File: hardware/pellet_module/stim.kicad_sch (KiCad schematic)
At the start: 17 parts, among them J11 Conn_Coaxial, J12 Conn_01x02_Pin, J13 Conn_01x02_Pin, J14 Conn_01x02_Pin, J15 Conn_Coaxial, J16 Conn_Coaxial, J17 Conn_Coaxial, J18 Conn_Coaxial, J21 Conn_Coaxial, U7 TXB0104RUT

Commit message: make updated pellet step for alogus
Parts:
- J12, J13, J14: footprint Connector_PinHeader_2.54mm:PinHeader_1x02_P2.54mm_Horizontal -> Connector_Molex:Molex_PicoBlade_53048-0210_1x02_P1.25mm_Horizontal; LCSC C225269 -> C505099; MPN A2005WR-2P -> 0530480210
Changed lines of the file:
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@@
+	(symbol
+		(lib_id "Connector:Conn_01x02_Pin")
+		(at 59.69 116.84 0)
+		(mirror y)
+		(unit 1)
+		(exclude_from_sim no)
+		(in_bom yes)
+		(on_board yes)
+		(dnp no)
+		(fields_autoplaced yes)
+		(property "Reference" "J14"
+			(at 60.96 116.8399 0)
+			(effects
+				(font
+					(size 1.27 1.27)
+				)
+				(justify right)
+			)
+		)
+		(property "Value" "Conn_01x02_Pin"
+			(at 60.96 119.3799 0)
+			(effects
+				(font
+					(size 1.27 1.27)
+				)
+				(justify right)
+			)
+		)
+		(property "Footprint" "Connector_Molex:Molex_PicoBlade_53048-0210_1x02_P1.25mm_Horizontal"
+			(at 59.69 116.84 0)
+			(effects
+				(font
+					(size 1.27 1.27)
+				)
+				(hide yes)
+			)
+		)
+		(property "Datasheet" "~"
+			(at 59.69 116.84 0)
+			(effects
+				(font
+					(size 1.27 1.27)
+				)
+				(hide yes)
+			)
+		)
+		(property "Description" "Generic connector, single row, 01x02, script generated"
+			(at 59.69 116.84 0)
+			(effects
+				(font
+					(size 1.27 1.27)
+				)
+				(hide yes)
+			)
+		)
+		(property "MPN" "0530480210"
+			(at 59.69 116.84 0)
+			(effects
+				(font
+					(size 1.27 1.27)
+				)
+				(hide yes)
+			)
+		)
+		(property "LCSC" "C505099"
+			(at 59.69 116.84 0)
+			(effects
+				(font
+					(size 1.27 1.27)
+				)
+				(hide yes)
+			)
+		)
+		(pin "2"
+		)
+		(pin "1"
+		)
+		(instances
+			(project "pellet"
+				(path "/48650363-a452-429d-997e-1ddabb69aad0/b8597be6-0cb3-4e54-9f55-240b87344e85"
+					(reference "J14")
+					(unit 1)
+				)
+			)
+		)
+	)
 	(symbol
 		(lib_id "Connector:Conn_01x02_Pin")
@@
 			)
 		)
-		(property "Footprint" "Connector_PinHeader_2.54mm:PinHeader_1x02_P2.54mm_Horizontal"
+		(property "Footprint" "Connector_Molex:Molex_PicoBlade_53048-0210_1x02_P1.25mm_Horizontal"
 			(at 59.69 101.6 0)
 			(effects
@@
 			)
 		)
-		(property "MPN" " A2005WR-2P"
+		(property "MPN" "0530480210"
 			(at 59.69 101.6 0)
 			(effects
@@
 			)
 		)
-		(property "LCSC" "C225269"
+		(property "LCSC" "C505099"
 			(at 59.69 101.6 0)
 			(effects
@@
 			)
 		)
-		(property "Footprint" "Connector_PinHeader_2.54mm:PinHeader_1x02_P2.54mm_Horizontal"
+		(property "Footprint" "Connector_Molex:Molex_PicoBlade_53048-0210_1x02_P1.25mm_Horizontal"
 			(at 59.69 86.36 0)
 			(effects
@@
 			)
 		)
-		(property "MPN" " A2005WR-2P"
+		(property "MPN" "0530480210"
 			(at 59.69 86.36 0)
 			(effects
@@
 			)
 		)
-		(property "LCSC" "C225269"
+		(property "LCSC" "C505099"
 			(at 59.69 86.36 0)
 			(effects
@@
 					(unit 1)
 				)
-			)
-		)
-	)
-	(symbol
-		(lib_id "Connector:Conn_01x02_Pin")
-		(at 59.69 116.84 0)
-		(mirror y)
-		(unit 1)
-		(exclude_from_sim no)
-		(in_bom yes)
-		(on_board yes)
-		(dnp no)
-		(fields_autoplaced yes)
-		(property "Reference" "J14"
-			(at 60.96 116.8399 0)
-			(effects
-				(font
-					(size 1.27 1.27)
-				)
-				(justify right)
-			)
-		)
-		(property "Value" "Conn_01x02_Pin"
-			(at 60.96 119.3799 0)
-			(effects
-				(font
-					(size 1.27 1.27)
-				)
-				(justify right)
-			)
-		)
-		(property "Footprint" "Connector_PinHeader_2.54mm:PinHeader_1x02_P2.54mm_Horizontal"
-			(at 59.69 116.84 0)
-			(effects
-				(font
-					(size 1.27 1.27)
-				)
-				(hide yes)
-			)
-		)
-		(property "Datasheet" "~"
-			(at 59.69 116.84 0)
-			(effects
-				(font
-					(size 1.27 1.27)
-				)
-				(hide yes)
-			)
-		)
-		(property "Description" "Generic connector, single row, 01x02, script generated"
-			(at 59.69 116.84 0)
-			(effects
-				(font
-					(size 1.27 1.27)
-				)
-				(hide yes)
-			)
-		)
-		(property "MPN" " A2005WR-2P"
-			(at 59.69 116.84 0)
-			(effects
-				(font
-					(size 1.27 1.27)
-				)
-				(hide yes)
-			)
-		)
-		(property "LCSC" "C225269"
-			(at 59.69 116.84 0)
-			(effects
-				(font
-					(size 1.27 1.27)
-				)
-				(hide yes)
-			)
-		)
-		(pin "2"
-		)
-		(pin "1"
-		)
-		(instances
-			(project "pellet"
-				(path "/48650363-a452-429d-997e-1ddabb69aad0/b8597be6-0cb3-4e54-9f55-240b87344e85"
-					(reference "J14")
-					(unit 1)
-				)

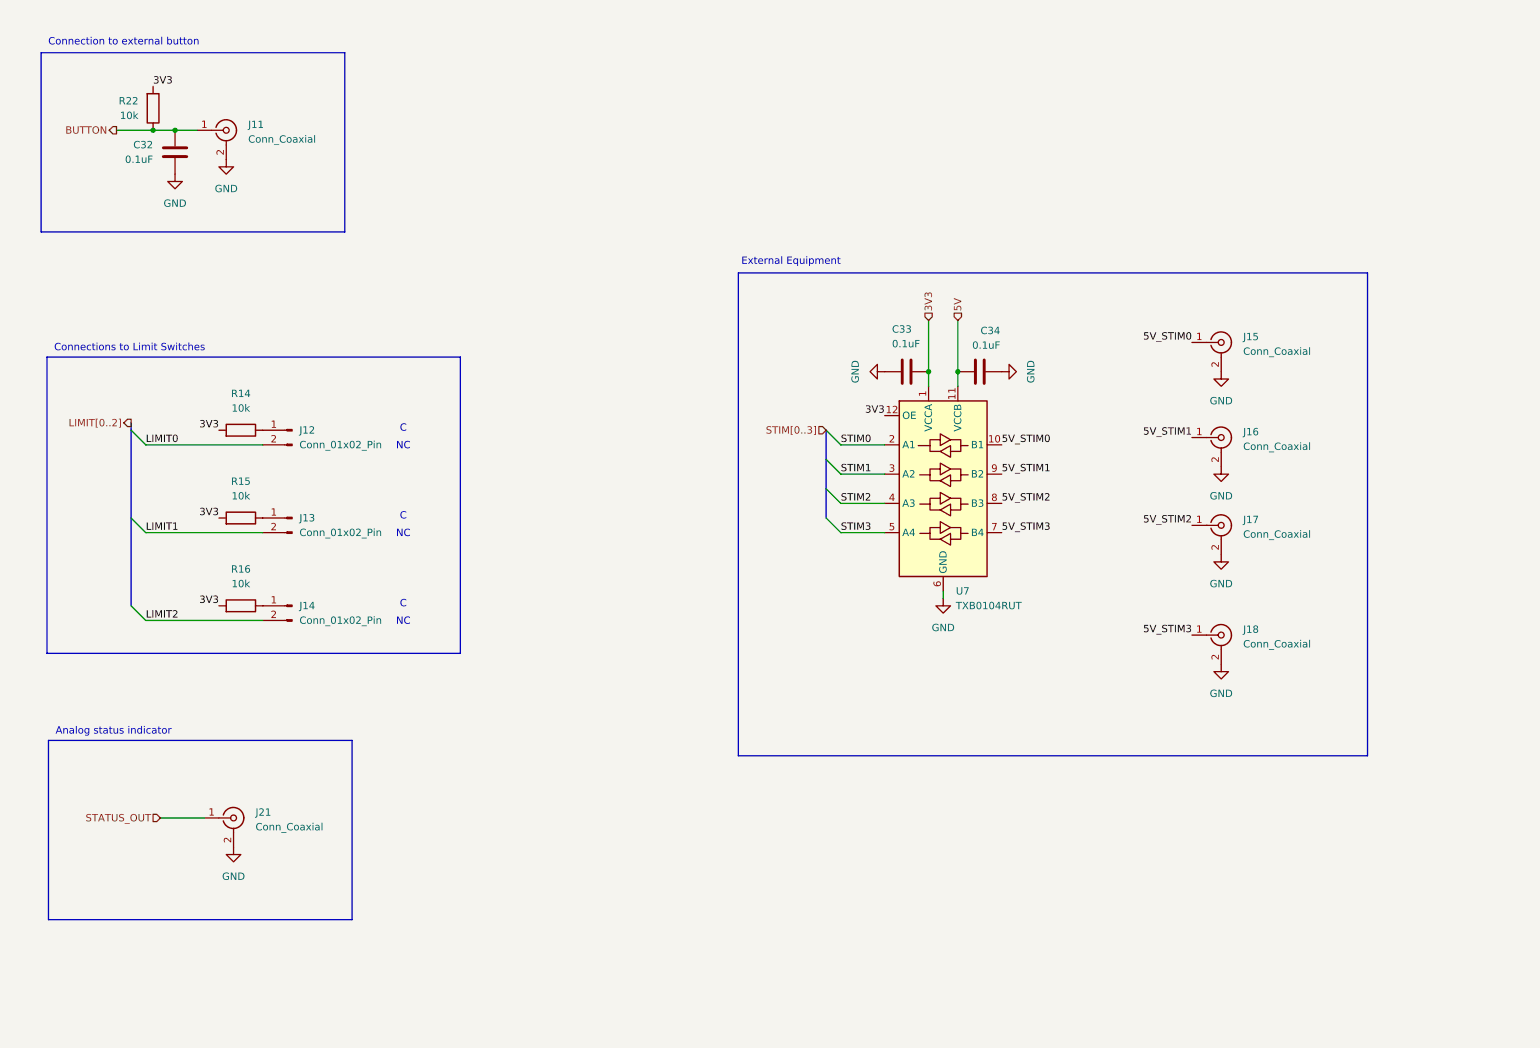
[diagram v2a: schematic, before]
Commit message: add test points to schematic
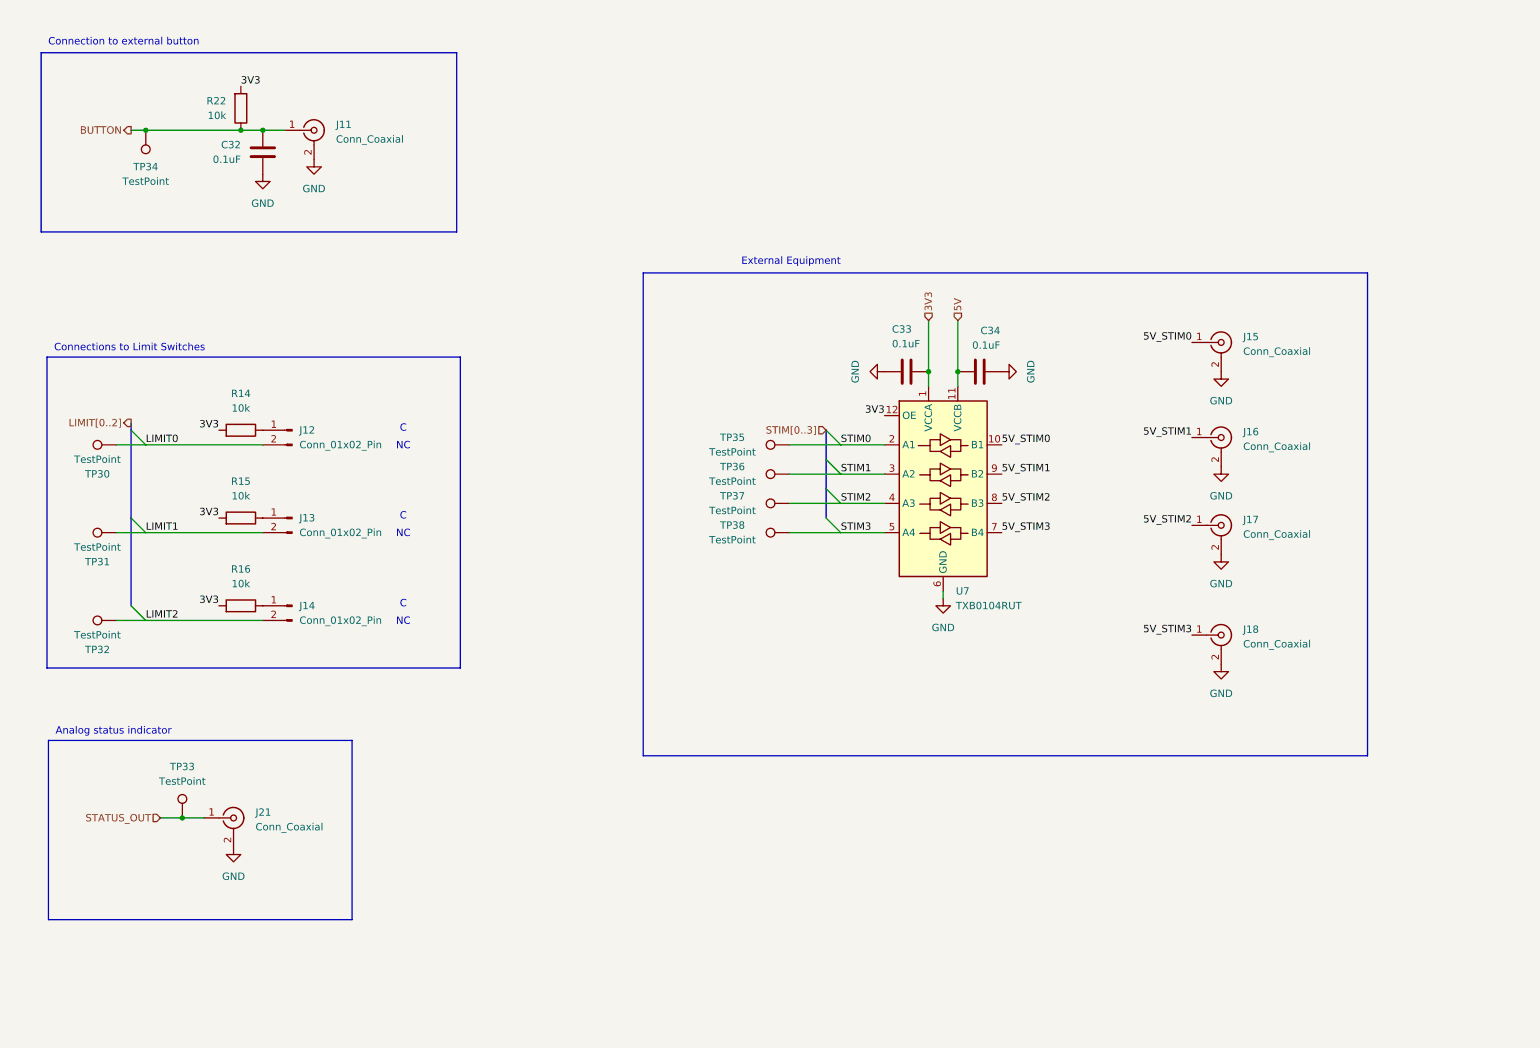
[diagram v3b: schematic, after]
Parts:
- added TP30, TP31, TP32, TP33, TP34, TP35, TP36, TP37, TP38: TestPoint, TestPoint:TestPoint_Pad_1.0x1.0mm, symbol Connector:TestPoint
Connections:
- net BUTTON: now also TP34.1
- net LIMIT0: now also TP30.1
- net LIMIT1: now also TP31.1
- net LIMIT2: now also TP32.1
- net STATUS_OUT: now also TP33.1
- net STIM0: now also TP35.1
- net STIM1: now also TP36.1
- net STIM2: now also TP37.1
- net STIM3: now also TP38.1
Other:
- moved on the sheet: C32, J11, R22

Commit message: Finish Alogus-requested changes (adding door sensors & led driver)
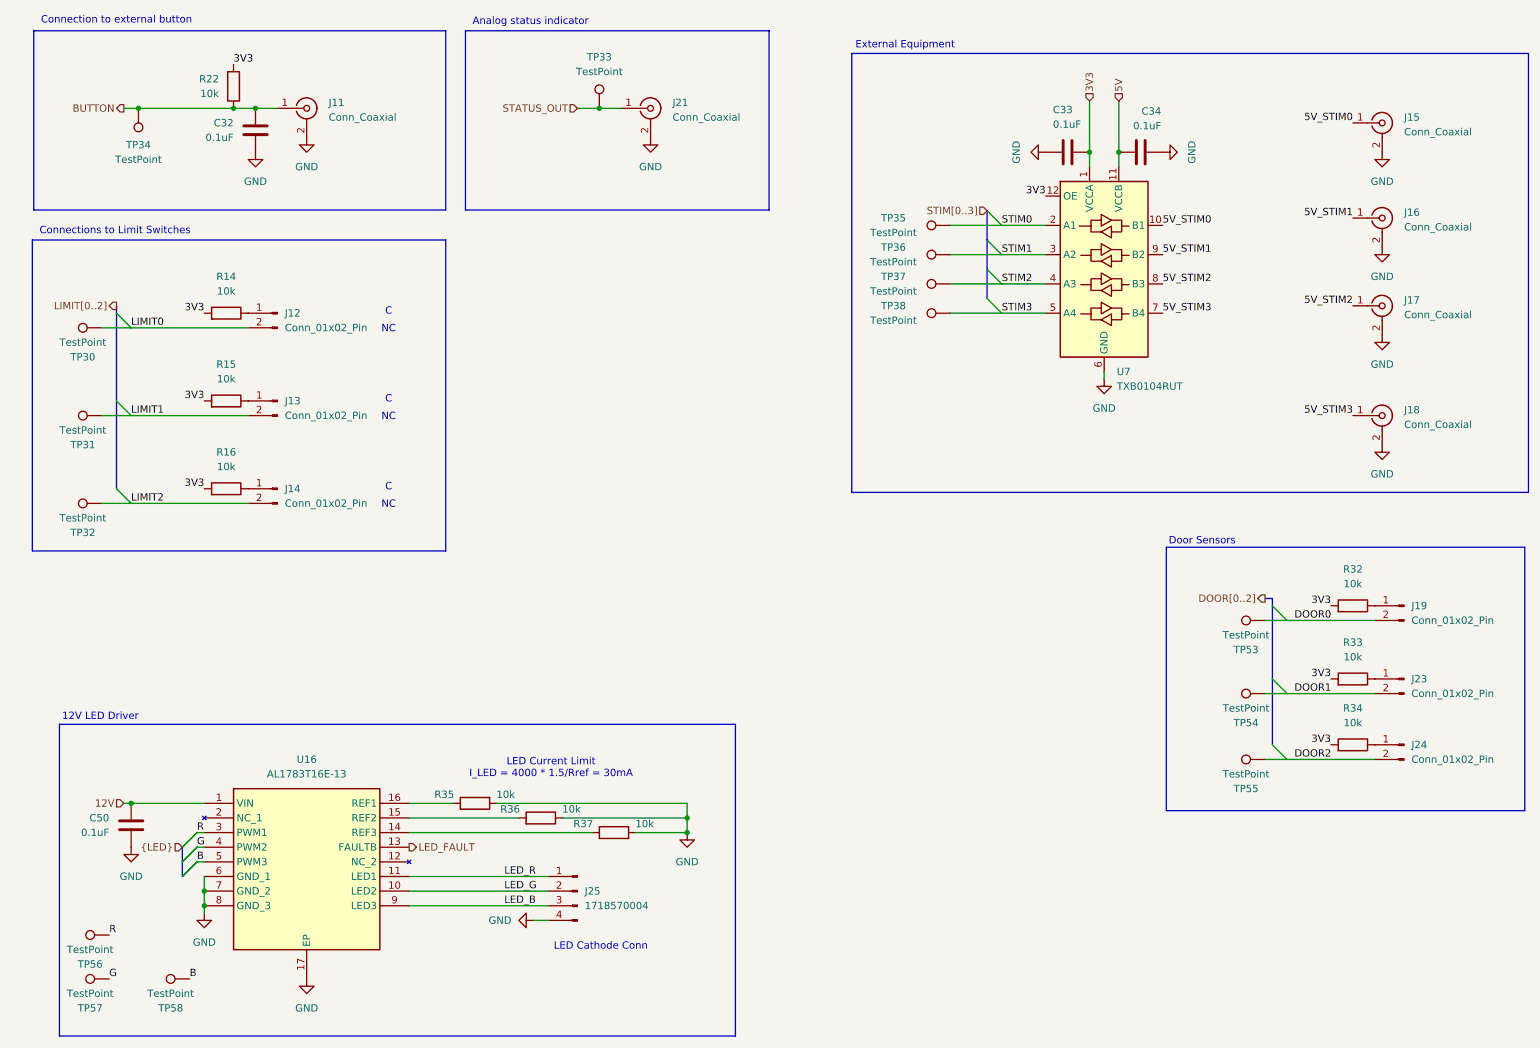
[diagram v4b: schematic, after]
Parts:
- added C50: 0.1uF, Capacitor_SMD:C_0603_1608Metric, symbol Device:C
- added J19, J23, J24: Conn_01x02_Pin, Connector_Molex:Molex_PicoBlade_53048-0210_1x02_P1.25mm_Horizontal, symbol Connector:Conn_01x02_Pin
- added J25: 1718570004, Leaf_Connectors:MOLEX_KK_171857-0004, symbol Connector:Conn_01x04_Pin
- added R32, R33, R34, R35, R36, R37: 10k, Resistor_SMD:R_0603_1608Metric, symbol Device:R
- added TP53, TP54, TP55, TP56, TP57, TP58: TestPoint, TestPoint:TestPoint_Pad_1.0x1.0mm, symbol Connector:TestPoint
- added U16: AL1783T16E-13, Leaf_LEDs:SOP65P640X108-17N, symbol Leaf_LEDs:AL1783T16E-13
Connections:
- net 3V3: now also R32.2, R33.2, R34.2
- net GND: now also C50.2, J25.4 (Pin_4), R35.1, R36.1, R37.1, U16.17 (EP), U16.6 (GND_1), U16.7 (GND_2), U16.8 (GND_3)
- new net: J24.1 (Pin_1), R34.1
- new net: R37.2, U16.14 (REF3)
- new net: R36.2, U16.15 (REF2)
- new net: R35.2, U16.16 (REF1)
- new net: J23.1 (Pin_1), R33.1
- new net: J19.1 (Pin_1), R32.1
- new net 12V: C50.1, U16.1 (VIN)
- new net B: TP58.1, U16.5 (PWM3)
- new net DOOR0: J19.2 (Pin_2), TP53.1
- new net DOOR1: J23.2 (Pin_2), TP54.1
- new net DOOR2: J24.2 (Pin_2), TP55.1
- new net G: TP57.1, U16.4 (PWM2)
- new net LED_B: J25.3 (Pin_3), U16.9 (LED3)
- new net LED_FAULT: U16.13 (FAULTB)
- new net LED_G: J25.2 (Pin_2), U16.10 (LED2)
- new net LED_R: J25.1 (Pin_1), U16.11 (LED1)
- new net R: TP56.1, U16.3 (PWM1)
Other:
- note added: "12V LED Driver"
- note added: "Door Sensors"
- note added: "LED Cathode Conn"
- note added: "LED Current Limit I_LED = 4000 * 1.5/Rref = 30mA"
- moved on the sheet: C32, C33, C34, J11, J12, J13, J14, J15, J16, J17, J18, J21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
